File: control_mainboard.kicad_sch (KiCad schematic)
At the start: 52 parts, among them J1 USB_C_Receptacle_USB2.0_14P, J2 [battery], J3 SD_Card_Receptacle, J4 [bootstrap jumper], J8 FFC Connector, Q1 DMG3415, Q2 DMG3415, SW1 [reset button], SW5 SW_SPST, U1 RP2040, U2 XC6220B331MR, U3 MCP73831-2-OT, U4 W25Q128JVS, Y1 ABM8-272-T3

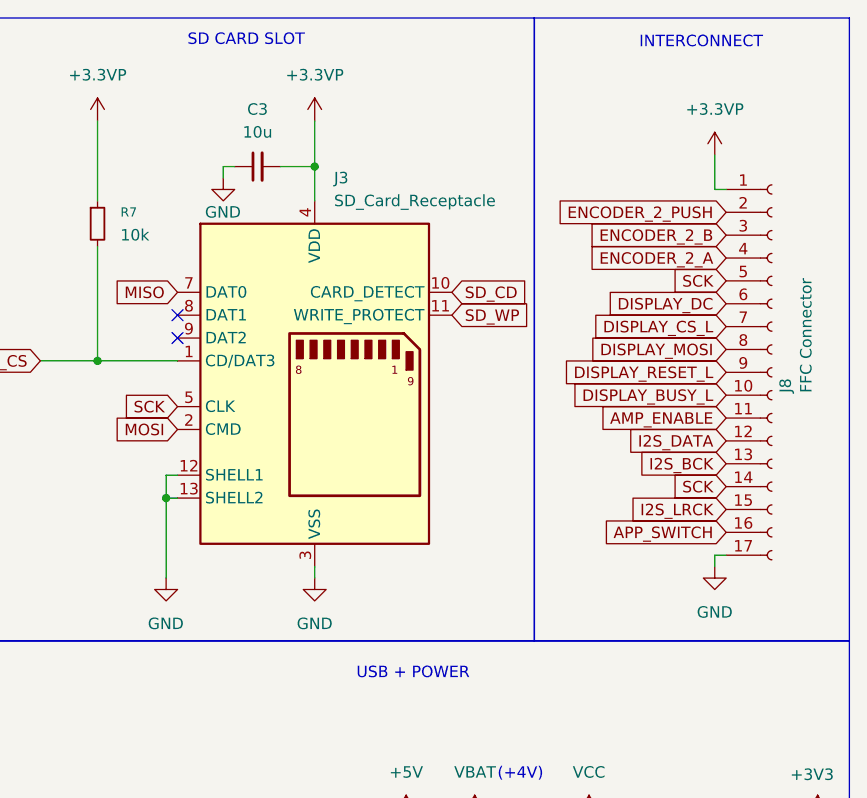
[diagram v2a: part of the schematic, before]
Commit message: assigning pcb footprints
assigned pcb footprints to most components:

- rotary encoder footprint will need slight modification to fit bourns PEC11L

- need to finalize components for reset button and the four switches before assigning those footprints
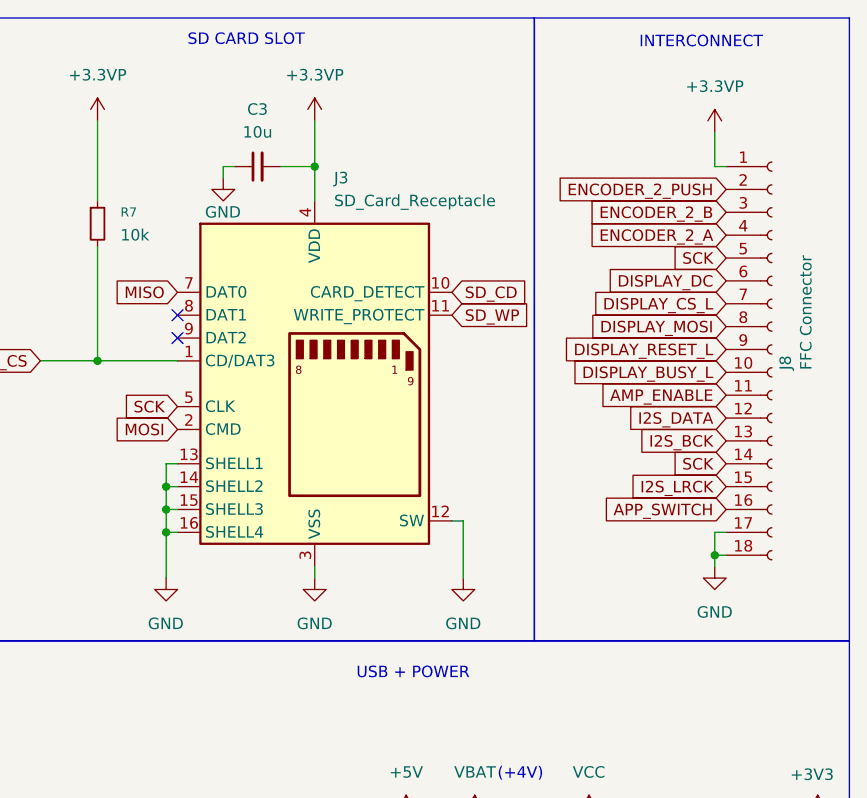
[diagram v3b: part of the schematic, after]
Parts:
- C1, C16, C17, C2, C3, C6, C8: footprint (none) -> Capacitor_SMD:C_0805_2012Metric
- C10, C11, C12, C13, C14, C15, C4, C5, C7, C9: footprint (none) -> Capacitor_SMD:C_1206_3216Metric
- J1: footprint (none) -> Connector_USB:USB_C_Receptacle_GCT_USB4105-xx-A_16P_TopMnt_Horizontal
- J2: footprint (none) -> Connector_JST:JST_PH_S2B-PH-K_1x02_P2.00mm_Horizontal
- J3: footprint (none) -> Connector_Card:SD_Hirose_DM1AA_SF_PEJ82
- J4: footprint (none) -> Connector_PinHeader_1.00mm:PinHeader_1x02_P1.00mm_Vertical
- J8: footprint (none) -> Connector_FFC-FPC:JUSHUO_AFA07-S18FCA-00_1x18-1MP_P1.0mm_Horizontal; symbol Connector:Conn_01x17_Socket -> Connector:Conn_01x18_Socket
- R1, R15, R2: footprint (none) -> Resistor_SMD:R_0805_2012Metric
- R10, R11, R12, R13, R14, R16, R29, R3, R30, R31, R39, R4, R7, R8, R9: footprint (none) -> Resistor_SMD:R_1206_3216Metric
- R5, R6: footprint (none) -> Resistor_SMD:R_0603_1608Metric
- Y1: footprint (none) -> Crystal:Crystal_SMD_3225-4Pin_3.2x2.5mm
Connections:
- net GND: now also J3.14 (SHELL2), J3.15 (SHELL3), J3.16 (SHELL4), J8.18 (Pin_18)

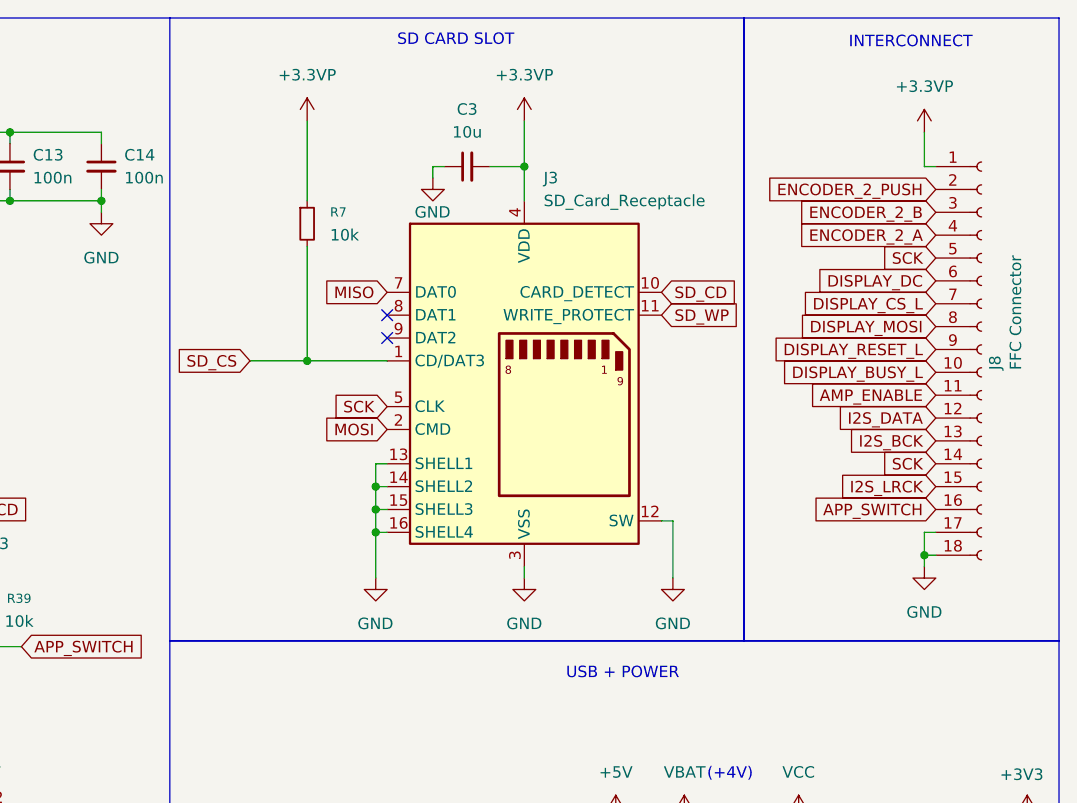
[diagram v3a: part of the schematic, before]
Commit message: finalizing schematics
connected the new DAC footprint, filled in title blocks
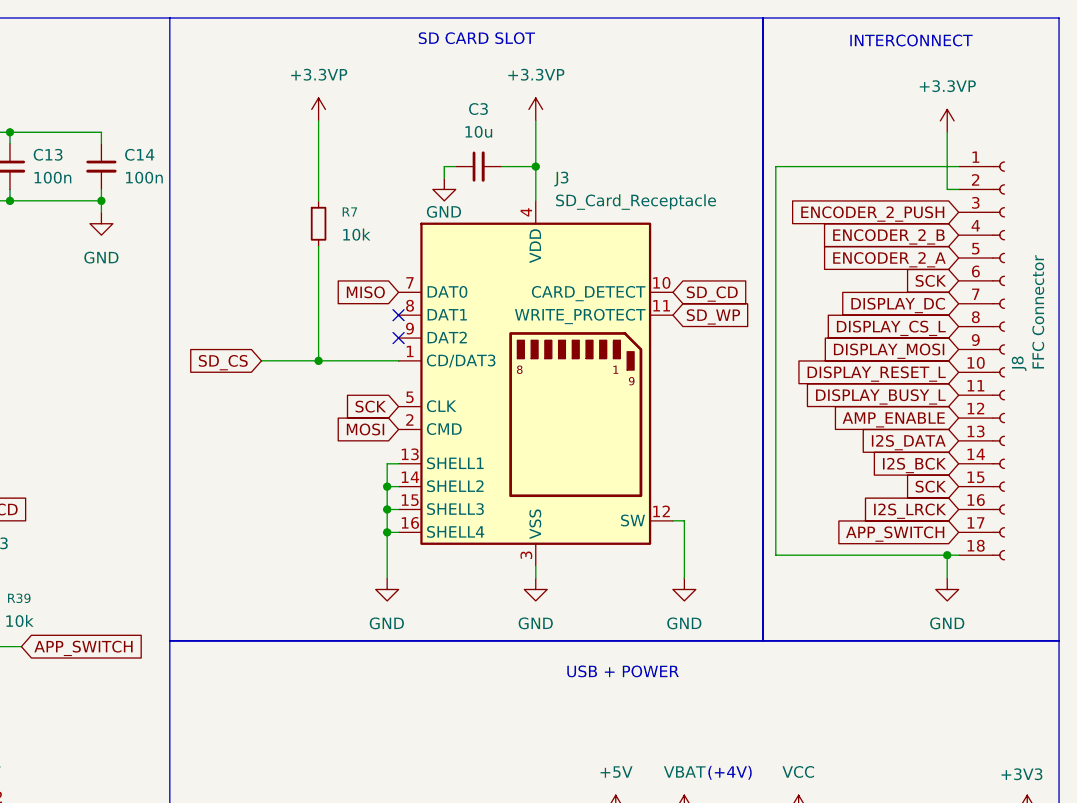
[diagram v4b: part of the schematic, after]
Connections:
- net +3.3VP: now also J8.2 (Pin_2); no longer J8.1 (Pin_1)
- net AMP_ENABLE: now also J8.12 (Pin_12); no longer J8.11 (Pin_11)
- net APP_SWITCH: now also J8.17 (Pin_17); no longer J8.16 (Pin_16)
- net DISPLAY_BUSY_L: now also J8.11 (Pin_11); no longer J8.10 (Pin_10)
- net DISPLAY_CS_L: now also J8.8 (Pin_8); no longer J8.7 (Pin_7)
- net DISPLAY_DC: now also J8.7 (Pin_7); no longer J8.6 (Pin_6)
- net DISPLAY_MOSI: now also J8.9 (Pin_9); no longer J8.8 (Pin_8)
- net DISPLAY_RESET_L: now also J8.10 (Pin_10); no longer J8.9 (Pin_9)
- net ENCODER_2_A: now also J8.5 (Pin_5); no longer J8.4 (Pin_4)
- net ENCODER_2_B: now also J8.4 (Pin_4); no longer J8.3 (Pin_3)
- net ENCODER_2_PUSH: now also J8.3 (Pin_3); no longer J8.2 (Pin_2)
- net GND: now also J8.1 (Pin_1); no longer J8.17 (Pin_17)
- net I2S_BCK: now also J8.14 (Pin_14); no longer J8.13 (Pin_13)
- net I2S_DATA: now also J8.13 (Pin_13); no longer J8.12 (Pin_12)
- net I2S_LRCK: now also J8.16 (Pin_16); no longer J8.15 (Pin_15)
- net SCK: now also J8.15 (Pin_15), J8.6 (Pin_6); no longer J8.14 (Pin_14), J8.5 (Pin_5)
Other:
- company: (none) -> rien+la_reine;
- title: (none) -> Tome: Control-Side Board
- moved on the sheet: C3, J3, J8, R7

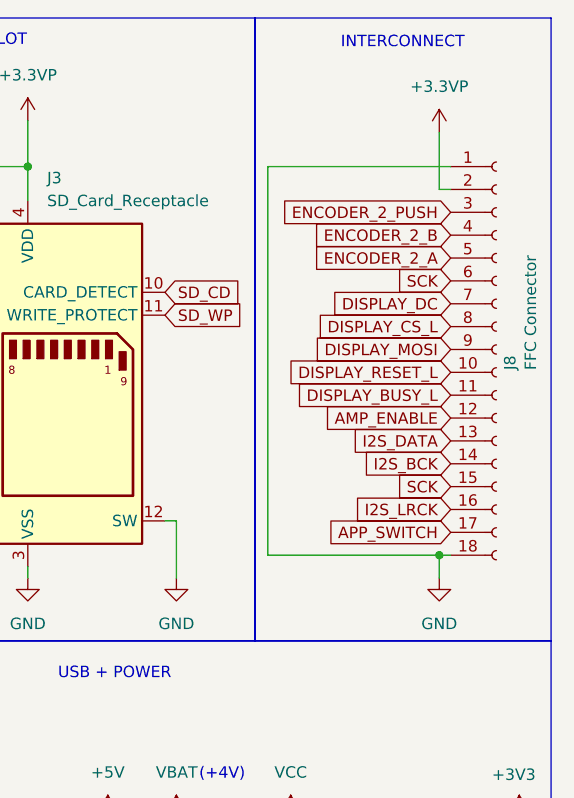
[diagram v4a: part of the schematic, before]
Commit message: corrected connector orientation
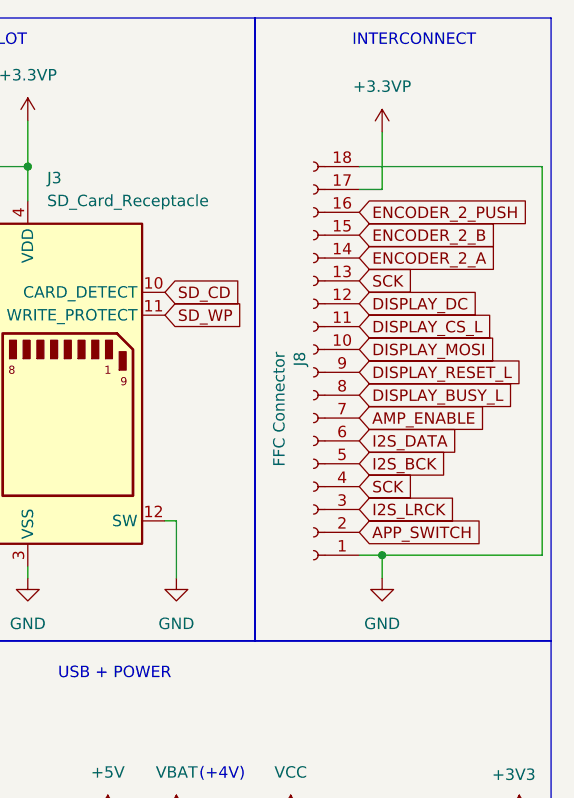
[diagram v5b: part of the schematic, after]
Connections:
- net +3.3VP: now also J8.17 (Pin_17); no longer J8.2 (Pin_2)
- net AMP_ENABLE: now also J8.7 (Pin_7); no longer J8.12 (Pin_12)
- net APP_SWITCH: now also J8.2 (Pin_2); no longer J8.17 (Pin_17)
- net DISPLAY_BUSY_L: now also J8.8 (Pin_8); no longer J8.11 (Pin_11)
- net DISPLAY_CS_L: now also J8.11 (Pin_11); no longer J8.8 (Pin_8)
- net DISPLAY_DC: now also J8.12 (Pin_12); no longer J8.7 (Pin_7)
- net DISPLAY_MOSI: now also J8.10 (Pin_10); no longer J8.9 (Pin_9)
- net DISPLAY_RESET_L: now also J8.9 (Pin_9); no longer J8.10 (Pin_10)
- net ENCODER_2_A: now also J8.14 (Pin_14); no longer J8.5 (Pin_5)
- net ENCODER_2_B: now also J8.15 (Pin_15); no longer J8.4 (Pin_4)
- net ENCODER_2_PUSH: now also J8.16 (Pin_16); no longer J8.3 (Pin_3)
- net I2S_BCK: now also J8.5 (Pin_5); no longer J8.14 (Pin_14)
- net I2S_DATA: now also J8.6 (Pin_6); no longer J8.13 (Pin_13)
- net I2S_LRCK: now also J8.3 (Pin_3); no longer J8.16 (Pin_16)
- net SCK: now also J8.13 (Pin_13), J8.4 (Pin_4); no longer J8.15 (Pin_15), J8.6 (Pin_6)
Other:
- moved on the sheet: J8

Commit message: assigned switch and reset button footprints
all footprints now assigned*

*will probably need something to connect the encoder daughterboard to the main boards
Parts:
- SW1: footprint (none) -> Button_Switch_SMD:Panasonic_EVQPUK_EVQPUB
- SW5: footprint (none) -> Button_Switch_SMD:SW_SPDT_CK_JS102011SAQN
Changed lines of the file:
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@@
 			)
 		)
-		(property "Footprint" ""
+		(property "Footprint" "Button_Switch_SMD:Panasonic_EVQPUK_EVQPUB"
 			(at 67.31 52.07 0)
 			(effects
@@
 			)
 		)
-		(property "Footprint" ""
+		(property "Footprint" "Button_Switch_SMD:SW_SPDT_CK_JS102011SAQN"
 			(at 162.56 100.33 0)
 			(effects

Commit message: switching to RP2350
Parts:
- removed U1: RP2040, Package_DFN_QFN:QFN-56-1EP_7x7mm_P0.4mm_EP3.2x3.2mm, symbol MCU_RaspberryPi:RP2040
- added C67, C68: 4.7u, Capacitor_SMD:C_0805_2012Metric, symbol Device:C_Small
- added J18: SM03B-SRSS-TB, Connector_JST:JST_SH_SM03B-SRSS-TB_1x03-1MP_P1.00mm_Horizontal, symbol Connector_Generic_MountingPin:Conn_01x03_MountingPin
- added L3: 3.3u, RP2350_80QFN_minimal:L_pol_2016, symbol Device:L
- added R40: 0, Resistor_SMD:R_0402_1005Metric, symbol Device:R
- added R?: 1k, Resistor_SMD:R_0603_1608Metric, symbol Device:R_Small
- added U8: RP2350B, Package_DFN_QFN:QFN-80-1EP_10x10mm_P0.4mm_EP3.4x3.4mm, symbol MCU_RaspberryPi:RP2350B
- C6: value 1u -> 4.7u
- C8: value 1u -> 10u
- R16: value 10k -> 33; footprint Resistor_SMD:R_1206_3216Metric -> Resistor_SMD:R_0603_1608Metric
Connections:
- net +1V1: now also C67.1, L3.1, U8.10 (DVDD), U8.32 (DVDD), U8.51 (DVDD), U8.65 (VREG_FB)
- net +3.3VP: now also C8.1
- net +3V3: now also R16.2, C68.1, U8.15 (IOVDD), U8.24 (IOVDD), U8.29 (IOVDD), U8.41 (IOVDD), U8.5 (IOVDD), U8.50 (IOVDD), U8.59 (ADC_AVDD), U8.60 (IOVDD), U8.64 (VREG_VIN), U8.68 (USB_OTP_VDD), U8.69 (QSPI_IOVDD), U8.76 (IOVDD); no longer C8.1, R16.1
- net FLASH_CS: now also R40.1
- net GND: now also C67.2, C68.2, J18.2 (Pin_2), J18.MP (MountPin), R?.1, U8.62 (VREG_PGND), U8.81 (GND); no longer SW1.1
- net at U4.2 (DO/IO_{1}): now also U8.74 (QSPI_SD1)
- net at U4.3 (~{WP}/IO_{2}): now also U8.73 (QSPI_SD2)
- net at U4.5 (DI/IO_{0}): now also U8.72 (QSPI_SD0)
- net QSPI_SCLK: now reaches U4.6 (CLK)
- net QSPI_SCLK: now also U8.71 (QSPI_SCLK)
- net at U4.7 (~{HOLD}/~{RESET}/IO_{3}): now also U8.70 (QSPI_SD3)
- net at C17.1, Y1.1: now also U8.30 (XIN)
- net at SW1.2: now also U8.35 (RUN); no longer R16.2
- net at R10.2: now also U8.31 (XOUT)
- net at R6.2: now also U8.67 (USB_DP)
- net at R5.2: now also U8.66 (USB_DM)
- new net: R?.2, SW1.1
- new net: R40.2, U8.75 (~{QSPI_SS})
- new net: J18.1 (Pin_1), U8.33 (SWCLK)
- new net: J18.3 (Pin_3), U8.34 (SWDIO)
- new net VREG_AVDD: C14.1, R16.1, U8.61 (VREG_AVDD)
- new net VREG_LX: L3.2, U8.63 (VREG_LX)
- no-connect marks 4 -> 2
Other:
- note added: "DEBUG CONNECTOR"
- note added: "RP2350(B) + FLASH + CRYSTAL"
- note added: "power circuitry needs to be placed very carefully, recommended to just follow the RP2350 minimal design exactly."
- note removed: "C6 should be close to RP2040 pin 45"
- note removed: "C8 should be close to RP2040 pin 44"
- note removed: "RP2040 + FLASH + CRYSTAL"
- moved on the sheet: C1, C10, C11, C12, C13, C15, C16, C17, C2, C3, C4, C5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

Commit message: wiring write protect to card detect
need to reduce GPIO pins used so wiring write protect on the SD card port to lock card detect high directly instead of connecting to the microcontroller. this should prevent the card from being detected at all if it's write protected, which is important because we cannot write bookmarks into a card that is read only (and I don't want to make a read-only mode, I don't see a reason to write protect a books/audio files card anyway)
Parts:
- removed R29, R39: 10k, Resistor_SMD:R_1206_3216Metric, symbol Device:R_Small
- removed U8: RP2350B, Package_DFN_QFN:QFN-80-1EP_10x10mm_P0.4mm_EP3.4x3.4mm, symbol MCU_RaspberryPi:RP2350B
- added C14: 100n, Capacitor_SMD:C_1206_3216Metric, symbol Device:C_Small
- added D9: LED, symbol Device:LED
- added Q?: Si1308EDL, Package_TO_SOT_SMD:SOT-323_SC-70, symbol Transistor_FET:Si1308EDL
- added U1: RP2350A, Package_DFN_QFN:QFN-60-1EP_7x7mm_P0.4mm_EP3.4x3.4mm, symbol MCU_RaspberryPi:RP2350A
- C?: renamed from C14; value 100n -> 4.7u
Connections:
- net +1V1: now also U1.23 (DVDD), U1.39 (DVDD), U1.50 (VREG_FB), U1.6 (DVDD)
- net +3.3VP: no longer R30.1
- net +3V3: now also R30.1, C14.1, U1.1 (IOVDD), U1.11 (IOVDD), U1.20 (IOVDD), U1.30 (IOVDD), U1.38 (IOVDD), U1.44 (ADC_AVDD), U1.45 (IOVDD), U1.49 (VREG_VIN), U1.53 (USB_OTP_VDD), U1.54 (QSPI_IOVDD); no longer C?.1
- net AMP_ENABLE: now also U1.32 (GPIO20)
- net BATT_MONITOR: now also U1.42 (GPIO28/ADC2)
- net BUS_MONITOR: now also U1.43 (GPIO29/ADC3)
- net DISPLAY_BUSY_L: now also U1.12 (GPIO8)
- net DISPLAY_BUSY_R: now also U1.16 (GPIO12)
- net DISPLAY_CS_L: now also U1.13 (GPIO9)
- net DISPLAY_CS_R: now also U1.17 (GPIO13)
- net DISPLAY_DC: now also U1.18 (GPIO14)
- net DISPLAY_MOSI: now also U1.15 (GPIO11)
- net DISPLAY_RESET_L: now also U1.19 (GPIO15)
- net DISPLAY_RESET_R: now also U1.27 (GPIO16)
- net ENCODER_1_A: now also U1.33 (GPIO21)
- net ENCODER_1_B: now also U1.34 (GPIO22)
- net ENCODER_1_PUSH: now also U1.35 (GPIO23)
- net ENCODER_2_A: now also U1.36 (GPIO24)
- net ENCODER_2_B: now also U1.37 (GPIO25)
- net ENCODER_2_PUSH: now also U1.40 (GPIO26/ADC0)
- net GND: now also C14.2, U1.47 (VREG_PGND), U1.61 (GND)
- net I2S_BCK: now also U1.29 (GPIO18)
- net I2S_DATA: now also U1.31 (GPIO19)
- net I2S_LRCK: now also J8.4 (Pin_4), U1.28 (GPIO17); no longer J8.3 (Pin_3)
- net PERIPHERAL_ENABLE: now also U1.41 (GPIO27/ADC1)
- net QSPI_SCLK: now also U1.56 (QSPI_SCLK)
- net SCK: now also U1.14 (GPIO10); no longer J8.4 (Pin_4)
- net SD_CD: now also Q?.2 (S); no longer R30.2
- net SD_WP: now also R31.2, Q?.1 (G)
- net STAT: no longer R11.2
- net VREG_AVDD: now also U1.46 (VREG_AVDD)
- net VREG_LX: now also U1.48 (VREG_LX)
- net at U4.2 (DO/IO_{1}): now also U1.59 (QSPI_SD1)
- net at U4.3 (~{WP}/IO_{2}): now also U1.58 (QSPI_SD2)
- net at U4.5 (DI/IO_{0}): now also U1.57 (QSPI_SD0)
- net at U4.7 (~{HOLD}/~{RESET}/IO_{3}): now also U1.55 (QSPI_SD3)
- net at C17.1, Y1.1: now also U1.21 (XIN)
- net at SW1.2: now also U1.26 (RUN)
- net at R40.2: now also U1.60 (~{QSPI_SS})
- net at R10.2: now also U1.22 (XOUT)
- net at J18.1 (Pin_1): now also U1.24 (SWCLK)
- net at J18.3 (Pin_3): now also U1.25 (SWDIO)
- net at R5.2: now also U1.51 (USB_DM)
- net at R6.2: now also U1.52 (USB_DP)
- net at SW5.1 (A): now also R11.2, U1.2 (GPIO0); no longer R31.2
- net APP_SWITCH: no longer names the net of J8.2 (Pin_2)
- new net CARD_DETECT: Q?.3 (D), R30.2, U1.3 (GPIO1)
- new net SD_CLK: U1.4 (GPIO2)
- new net SD_CMD: U1.5 (GPIO3)
- new net SD_D0: U1.7 (GPIO4)
- new net SD_D1: U1.8 (GPIO5)
- new net SD_D2: U1.9 (GPIO6)
- new net SD_D3: U1.10 (GPIO7)
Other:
- note added: "lock card detect high (card not detected) if write protect is enabled"
- note added: "make sure that the SPI's clock, MOSI and MISO lines are length match and run as close to each other on the layout as possible, with <0.5 mm of mismatch in length. good design practice for any fast-edge clock or driver circuits."
- moved on the sheet: R11, R30, SW5
